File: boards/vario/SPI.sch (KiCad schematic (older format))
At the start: 23 parts, among them Q2 Q_NMOS_GSD, U1 74HC273, U2 74LS161, U3 74HC74, U31 74LS14, U32 74LS32, U33 74LS08, U4 74HC273, U5 74LS151, U6 74HC244

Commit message: Vario: component names and footprints
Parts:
- C27, C28, C29, C30, C31, C32, C33, C34, C35, C36: footprint (none) -> Capacitor_SMD:C_0805_2012Metric
- D2: footprint (none) -> LED_SMD:LED_0805_2012Metric
- Q2: footprint (none) -> Package_TO_SOT_SMD:SOT-23
- R19, R5: footprint (none) -> Resistor_SMD:R_0805_2012Metric
- U1, U4: value 74HC273 -> 74HC273PW; footprint (none) -> Package_SO:TSSOP-20_4.4x6.5mm_P0.65mm
- U2: value 74LS161 -> 74HC161PW; footprint (none) -> Package_SO:TSSOP-16_4.4x5mm_P0.65mm
- U3: value 74HC74 -> 74HC74PW; footprint (none) -> Package_SO:TSSOP-14_4.4x5mm_P0.65mm
- U31: value 74LS14 -> SN74LV14APW; footprint (none) -> Package_SO:TSSOP-14_4.4x5mm_P0.65mm
- U32: value 74LS32 -> SN74HC32PWR; footprint (none) -> Package_SO:TSSOP-14_4.4x5mm_P0.65mm
- U33: value 74LS08 -> 74HC08PW; footprint (none) -> Package_SO:TSSOP-14_4.4x5mm_P0.65mm
- U5: value 74LS151 -> MC74HC151ADTR2G; footprint (none) -> Package_SO:TSSOP-16_4.4x5mm_P0.65mm
- U6: value 74HC244 -> MC74HC244ADT; footprint (none) -> Package_SO:TSSOP-20_4.4x6.5mm_P0.65mm

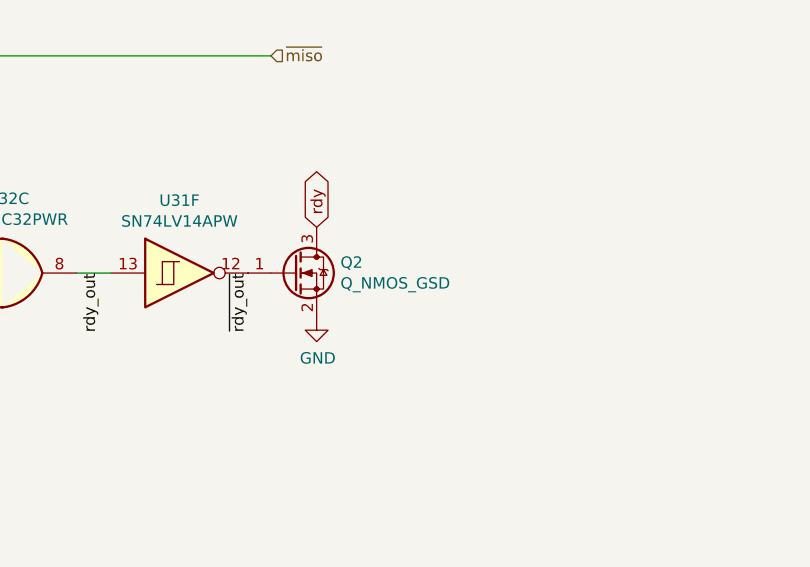
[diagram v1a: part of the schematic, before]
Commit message: Vario: transistors and capacitors
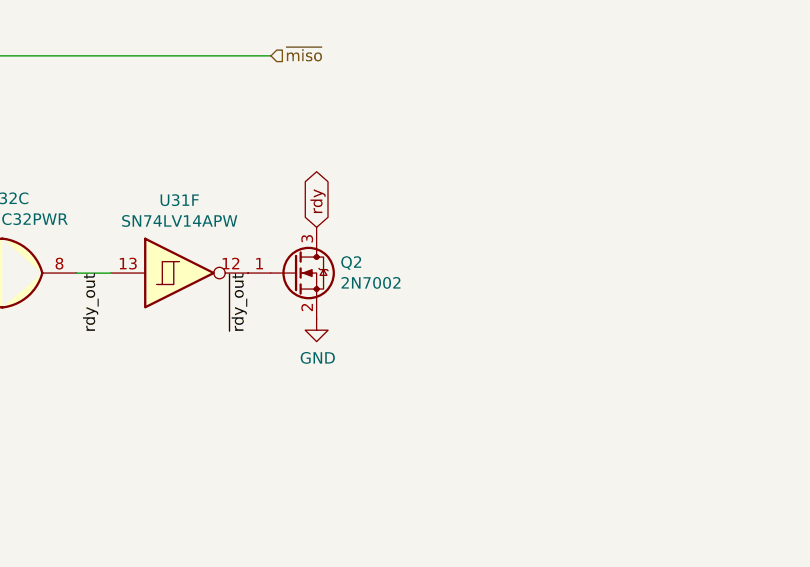
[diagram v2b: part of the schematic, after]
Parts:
- Q2: value Q_NMOS_GSD -> 2N7002
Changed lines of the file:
@@
 P 11400 3950
 F 0 "Q2" H 11604 3996 50  0000 L CNN
-F 1 "Q_NMOS_GSD" H 11604 3905 50  0000 L CNN
+F 1 "2N7002" H 11604 3905 50  0000 L CNN
 F 2 "Package_TO_SOT_SMD:SOT-23" H 11600 4050 50  0001 C CNN
 F 3 "~" H 11400 3950 50  0001 C CNN

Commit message: Vario: power nets
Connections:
- net d0: now also U1.13 (D4); no longer U1.3 (D0)
- net d1: now also U1.14 (D5); no longer U1.4 (D1)
- net d2: now also U1.17 (D6); no longer U1.7 (D2)
- net d3: now also U1.18 (D7); no longer U1.8 (D3)
- net d4: now also U1.3 (D0); no longer U1.13 (D4)
- net d5: now also U1.4 (D1); no longer U1.14 (D5)
- net d6: now also U1.7 (D2); no longer U1.17 (D6)
- net d7: now also U1.8 (D3); no longer U1.18 (D7)
- net reg_send_q0: now also U1.12 (Q4); no longer U1.2 (Q0)
- net reg_send_q1: now also U1.15 (Q5); no longer U1.5 (Q1)
- net reg_send_q2: now also U1.16 (Q6); no longer U1.6 (Q2)
- net reg_send_q3: now also U1.19 (Q7); no longer U1.9 (Q3)
- net reg_send_q4: now also U1.2 (Q0); no longer U1.12 (Q4)
- net reg_send_q5: now also U1.5 (Q1); no longer U1.15 (Q5)
- net reg_send_q6: now also U1.6 (Q2); no longer U1.16 (Q6)
- net reg_send_q7: now also U1.9 (Q3); no longer U1.19 (Q7)
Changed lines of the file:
@@
 	1    0    0    -1
 $EndComp
+Text Label 3950 4050 2    50   ~ 0
+d0
+Text Label 3950 4150 2    50   ~ 0
+d1
+Text Label 3950 4250 2    50   ~ 0
+d2
+Text Label 3950 4350 2    50   ~ 0
+d3
 Text Label 3950 3650 2    50   ~ 0
-d0
+d4
 Text Label 3950 3750 2    50   ~ 0
-d1
+d5
 Text Label 3950 3850 2    50   ~ 0
-d2
+d6
 Text Label 3950 3950 2    50   ~ 0
-d3
-Text Label 3950 4050 2    50   ~ 0
-d4
-Text Label 3950 4150 2    50   ~ 0
-d5
-Text Label 3950 4250 2    50   ~ 0
-d6
-Text Label 3950 4350 2    50   ~ 0
 d7
+Text Label 4950 4050 0    50   ~ 0
+reg_send_q0
+Text Label 4950 4150 0    50   ~ 0
+reg_send_q1
+Text Label 4950 4250 0    50   ~ 0
+reg_send_q2
+Text Label 4950 4350 0    50   ~ 0
+reg_send_q3
 Text Label 4950 3650 0    50   ~ 0
-reg_send_q0
+reg_send_q4
 Text Label 4950 3750 0    50   ~ 0
-reg_send_q1
+reg_send_q5
 Text Label 4950 3850 0    50   ~ 0
-reg_send_q2
+reg_send_q6
 Text Label 4950 3950 0    50   ~ 0
-reg_send_q3
-Text Label 4950 4050 0    50   ~ 0
-reg_send_q4
-Text Label 4950 4150 0    50   ~ 0
-reg_send_q5
-Text Label 4950 4250 0    50   ~ 0
-reg_send_q6
-Text Label 4950 4350 0    50   ~ 0
 reg_send_q7
 $Comp
@@
 Wire Wire Line
 	6750 8500 7250 8500
-Wire Bus Line
-	1700 2050 1700 3050
 $Comp
 L Device:R R19
@@
 	0    -1   -1   0
 $EndComp
+Wire Bus Line
+	1700 2050 1700 3050
 $EndSCHEMATC

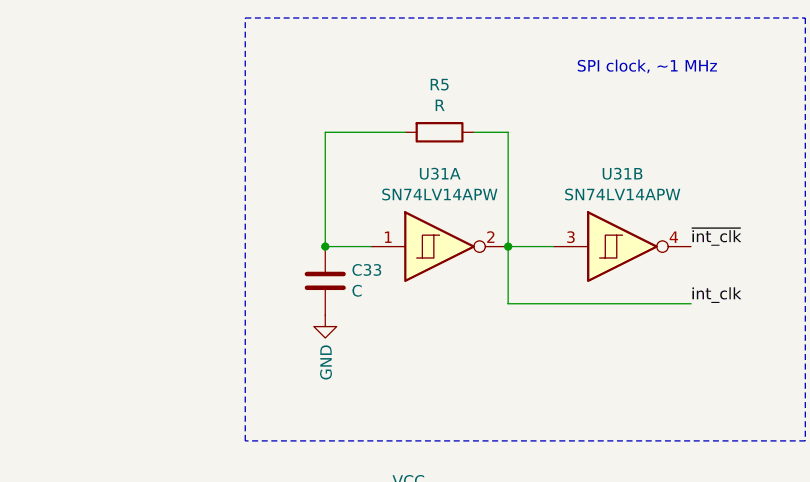
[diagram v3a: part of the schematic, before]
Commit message: Vario: exact RC values
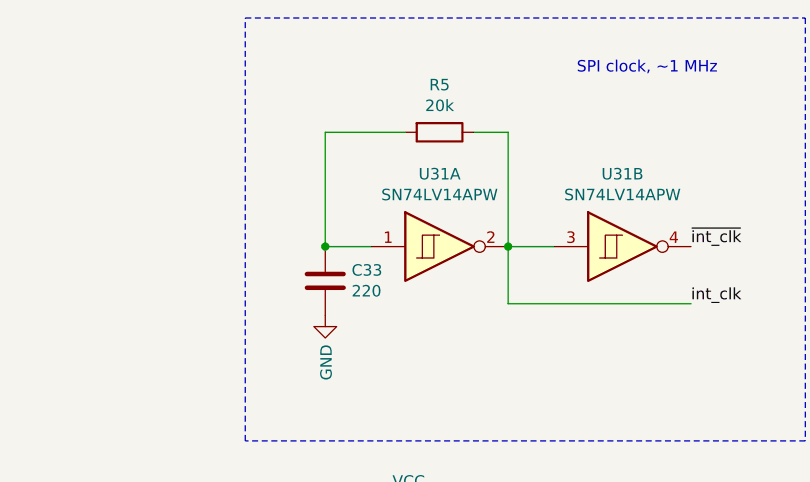
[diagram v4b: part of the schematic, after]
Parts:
- C33: value C -> 220
- R5: value R -> 20k
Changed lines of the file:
@@
 P 4400 1750
 F 0 "C33" H 4515 1796 50  0000 L CNN
-F 1 "C" H 4515 1705 50  0000 L CNN
+F 1 "220" H 4515 1705 50  0000 L CNN
 F 2 "Capacitor_SMD:C_0805_2012Metric" H 4438 1600 50  0001 C CNN
 F 3 "~" H 4400 1750 50  0001 C CNN
@@
 P 4900 1100
 F 0 "R5" V 4693 1100 50  0000 C CNN
-F 1 "R" V 4784 1100 50  0000 C CNN
+F 1 "20k" V 4784 1100 50  0000 C CNN
 F 2 "Resistor_SMD:R_0805_2012Metric" V 4830 1100 50  0001 C CNN
 F 3 "~" H 4900 1100 50  0001 C CNN
